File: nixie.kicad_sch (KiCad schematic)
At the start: 51 parts, among them J1 Barrel_Jack, Q1 2N3906, Q2 IRF644, U1 4504, U2 MC34063AP, U3 HV5222PG-G, U4 LM7805_TO220, U5 HV5222PG-G

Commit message: pcb layout update
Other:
- moved on the sheet: N10, N7, N8, N9

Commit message: pcb layout update
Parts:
- added J2: Conn_01x02_Pin, Connector_PinHeader_2.54mm:PinHeader_1x02_P2.54mm_Vertical, symbol Connector:Conn_01x02_Pin
- J1: footprint Connector_PinHeader_2.54mm:PinHeader_1x02_P2.54mm_Vertical -> TerminalBlock_Phoenix:TerminalBlock_Phoenix_MKDS-1,5-2-5.08_1x02_P5.08mm_Horizontal
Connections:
- net GND: now also J2.1 (Pin_1)
- net Vin: now also J2.2 (Pin_2)
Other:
- moved on the sheet: J1
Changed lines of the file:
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@@
 	)
 	(junction
-		(at 29.21 31.75)
+		(at 29.21 29.21)
 		(diameter 0)
 		(color 0 0 0 0)
@@
 	)
 	(junction
-		(at 29.21 26.67)
+		(at 29.21 24.13)
 		(diameter 0)
 		(color 0 0 0 0)
@@
 	(wire
 		(pts
-			(xy 27.94 26.67) (xy 29.21 26.67)
+			(xy 27.94 24.13) (xy 29.21 24.13)
 		)
 		(stroke
@@
 	(polyline
 		(pts
-			(xy 134.62 16.51) (xy 134.62 95.25)
+			(xy 134.62 14.478) (xy 134.62 95.25)
 		)
 		(stroke
@@
 	(wire
 		(pts
-			(xy 29.21 31.75) (xy 27.94 31.75)
+			(xy 29.21 29.21) (xy 27.94 29.21)
 		)
 		(stroke
@@
 	(wire
 		(pts
-			(xy 29.21 26.67) (xy 30.48 26.67)
+			(xy 29.21 24.13) (xy 30.48 24.13)
 		)
 		(stroke
@@
 	(polyline
 		(pts
-			(xy 283.21 16.51) (xy 134.62 16.51)
+			(xy 283.21 14.478) (xy 134.62 14.478)
 		)
 		(stroke
@@
 	(wire
 		(pts
-			(xy 29.21 25.4) (xy 29.21 26.67)
+			(xy 29.21 22.86) (xy 29.21 24.13)
 		)
 		(stroke
@@
 	(wire
 		(pts
-			(xy 29.21 33.02) (xy 29.21 31.75)
+			(xy 29.21 30.48) (xy 29.21 29.21)
 		)
 		(stroke
@@
 	(polyline
 		(pts
-			(xy 283.21 165.1) (xy 283.21 16.51)
+			(xy 283.21 165.1) (xy 283.21 14.478)
 		)
 		(stroke
@@
 	)
 	(rectangle
-		(start 12.7 16.51)
-		(end 132.08 92.71)
+		(start 12.7 14.478)
+		(end 132.08 90.678)
 		(stroke
 			(width 0.2)
@@
 		)
 	)
+	(global_label "Vin"
+		(shape output)
+		(at 35.56 36.83 0)
+		(fields_autoplaced yes)
+		(effects
+			(font
+				(size 1.27 1.27)
+			)
+			(justify left)
+		)
+		(property "Intersheetrefs" "${INTERSHEET_REFS}"
+			(at 41.3876 36.83 0)
+			(effects
+				(font
+					(size 1.27 1.27)
+				)
+				(justify left)
+				(hide yes)
+			)
+		)
+	)
 	(global_label "5V"
 		(shape output)
@@
 	(global_label "Vin"
 		(shape output)
-		(at 30.48 26.67 0)
+		(at 30.48 24.13 0)
 		(fields_autoplaced yes)
 		(effects
@@
 		)
 		(property "Intersheetrefs" "${INTERSHEET_REFS}"
-			(at 36.3076 26.67 0)
+			(at 36.3076 24.13 0)
 			(effects
 				(font
@@
 	(symbol
 		(lib_id "Connector:Barrel_Jack")
-		(at 20.32 29.21 0)
+		(at 20.32 26.67 0)
 		(unit 1)
 		(exclude_from_sim no)
@@
 		(fields_autoplaced yes)
 		(property "Reference" "J1"
-			(at 20.32 20.32 0)
+			(at 20.32 17.78 0)
 			(effects
 				(font
@@
 		)
 		(property "Value" "Barrel_Jack"
-			(at 20.32 22.86 0)
+			(at 20.32 20.32 0)
 			(effects
 				(font
@@
 			)
 		)
-		(property "Footprint" "Connector_PinHeader_2.54mm:PinHeader_1x02_P2.54mm_Vertical"
-			(at 21.59 30.226 0)
+		(property "Footprint" "TerminalBlock_Phoenix:TerminalBlock_Phoenix_MKDS-1,5-2-5.08_1x02_P5.08mm_Horizontal"
+			(at 21.59 27.686 0)
 			(effects
 				(font
@@
 		)
 		(property "Datasheet" "~"
-			(at 21.59 30.226 0)
+			(at 21.59 27.686 0)
 			(effects
 				(font
@@
 		)
 		(property "Description" "DC Barrel Jack"
-			(at 20.32 29.21 0)
+			(at 20.32 26.67 0)
 			(effects
 				(font
@@
 	(symbol
 		(lib_id "power:PWR_FLAG")
-		(at 29.21 25.4 0)
+		(at 29.21 22.86 0)
 		(unit 1)
 		(exclude_from_sim no)
@@
 		(fields_autoplaced yes)
 		(property "Reference" "#FLG01"
-			(at 29.21 23.495 0)
+			(at 29.21 20.955 0)
 			(effects
 				(font
@@
 		)
 		(property "Value" "PWR_FLAG"
-			(at 29.21 20.32 0)
+			(at 29.21 17.78 0)
 			(effects
 				(font
@@
 		)
 		(property "Footprint" ""
-			(at 29.21 25.4 0)
+			(at 29.21 22.86 0)
 			(effects
 				(font
@@
 		)
 		(property "Datasheet" "~"
-			(at 29.21 25.4 0)
+			(at 29.21 22.86 0)
 			(effects
 				(font
@@
 		)
 		(property "Description" "Special symbol for telling ERC where power comes from"
-			(at 29.21 25.4 0)
+			(at 29.21 22.86 0)
 			(effects
 				(font
@@
 	)
 	(symbol
+		(lib_id "Connector:Conn_01x02_Pin")
+		(at 30.48 39.37 0)
+		(mirror x)
+		(unit 1)
+		(exclude_from_sim no)
+		(in_bom yes)
+		(on_board yes)
+		(dnp no)
+		(fields_autoplaced yes)
+		(property "Reference" "J2"
+			(at 29.21 36.8299 0)
+			(effects
+				(font
+					(size 1.27 1.27)
+				)
+				(justify right)
+			)
+		)
+		(property "Value" "Conn_01x02_Pin"
+			(at 29.21 39.3699 0)
+			(effects
+				(font
+					(size 1.27 1.27)
+				)
+				(justify right)
+			)
+		)
+		(property "Footprint" "Connector_PinHeader_2.54mm:PinHeader_1x02_P2.54mm_Vertical"
+			(at 30.48 39.37 0)
+			(effects
+				(font
+					(size 1.27 1.27)
+				)
+				(hide yes)
+			)
+		)
+		(property "Datasheet" "~"
+			(at 30.48 39.37 0)
+			(effects
+				(font
+					(size 1.27 1.27)
+				)
+				(hide yes)
+			)
+		)
+		(property "Description" "Generic connector, single row, 01x02, script generated"
+			(at 30.48 39.37 0)
+			(effects
+				(font
+					(size 1.27 1.27)
+				)
+				(hide yes)
+			)
+		)
+		(pin "1"
+		)
+		(pin "2"
+		)
+		(instances
+			(project ""
+				(path "/4d215aa3-d175-40c4-bbb4-87e7c6a030b1"
+					(reference "J2")
+					(unit 1)
+				)
+			)
+		)
+	)
+	(symbol
 		(lib_id "power:GND")
-		(at 29.21 33.02 0)
+		(at 29.21 30.48 0)
 		(unit 1)
 		(exclude_from_sim no)
@@
 		(dnp no)
 		(property "Reference" "#PWR03"
-			(at 29.21 39.37 0)
+			(at 29.21 36.83 0)
 			(effects
 				(font
@@
 		)
 		(property "Value" "GND"
-			(at 29.21 37.084 0)
+			(at 29.21 34.544 0)
 			(effects
 				(font
@@
 		)
 		(property "Footprint" ""
-			(at 29.21 33.02 0)
+			(at 29.21 30.48 0)
 			(effects
 				(font
@@
 		)
 		(property "Datasheet" ""
-			(at 29.21 33.02 0)
+			(at 29.21 30.48 0)
 			(effects
 				(font
@@
 		)
 		(property "Description" "Power symbol creates a global label with name \"GND\" , ground"
-			(at 29.21 33.02 0)
+			(at 29.21 30.48 0)
 			(effects
 				(font
@@
 	(symbol
 		(lib_id "power:PWR_FLAG")
-		(at 29.21 31.75 270)
+		(at 29.21 29.21 270)
 		(unit 1)
 		(exclude_from_sim no)
@@
 		(fields_autoplaced yes)
 		(property "Reference" "#FLG02"
-			(at 31.115 31.75 0)
+			(at 31.115 29.21 0)
 			(effects
 				(font
@@
 		)
 		(property "Value" "PWR_FLAG"
-			(at 33.02 31.7499 90)
+			(at 33.02 29.2099 90)
 			(effects
 				(font
@@
 		)
 		(property "Footprint" ""
-			(at 29.21 31.75 0)
+			(at 29.21 29.21 0)
 			(effects
 				(font
@@
 		)
 		(property "Datasheet" "~"
-			(at 29.21 31.75 0)
+			(at 29.21 29.21 0)
 			(effects
 				(font
@@
 		)
 		(property "Description" "Special symbol for telling ERC where power comes from"
-			(at 29.21 31.75 0)
+			(at 29.21 29.21 0)
 			(effects
 				(font
@@
 					(unit 1)
 				)
+			)
+		)
+	)
+	(symbol
+		(lib_id "power:GND")
+		(at 35.56 39.37 0)
+		(unit 1)
+		(exclude_from_sim no)
+		(in_bom yes)
+		(on_board yes)
+		(dnp no)
+		(property "Reference" "#PWR032"
+			(at 35.56 45.72 0)
+			(effects
+				(font
+					(size 1.27 1.27)
+				)
+				(hide yes)
+			)
+		)
+		(property "Value" "GND"
+			(at 35.56 43.434 0)
+			(effects
+				(font
+					(size 1.27 1.27)
+				)
+			)
+		)
+		(property "Footprint" ""
+			(at 35.56 39.37 0)
+			(effects
+				(font
+					(size 1.27 1.27)
+				)
+				(hide yes)
+			)
+		)
+		(property "Datasheet" ""
+			(at 35.56 39.37 0)
+			(effects
+				(font
+					(size 1.27 1.27)
+				)
+				(hide yes)
+			)
+		)
+		(property "Description" "Power symbol creates a global label with name \"GND\" , ground"
+			(at 35.56 39.37 0)
+			(effects
+				(font
+					(size 1.27 1.27)
+				)
+				(hide yes)
+			)
+		)
+		(pin "1"
+		)
+		(instances
+			(project "nixie"
+				(path "/4d215aa3-d175-40c4-bbb4-87e7c6a030b1"
+					(reference "#PWR032")
+					(unit 1)
+				)

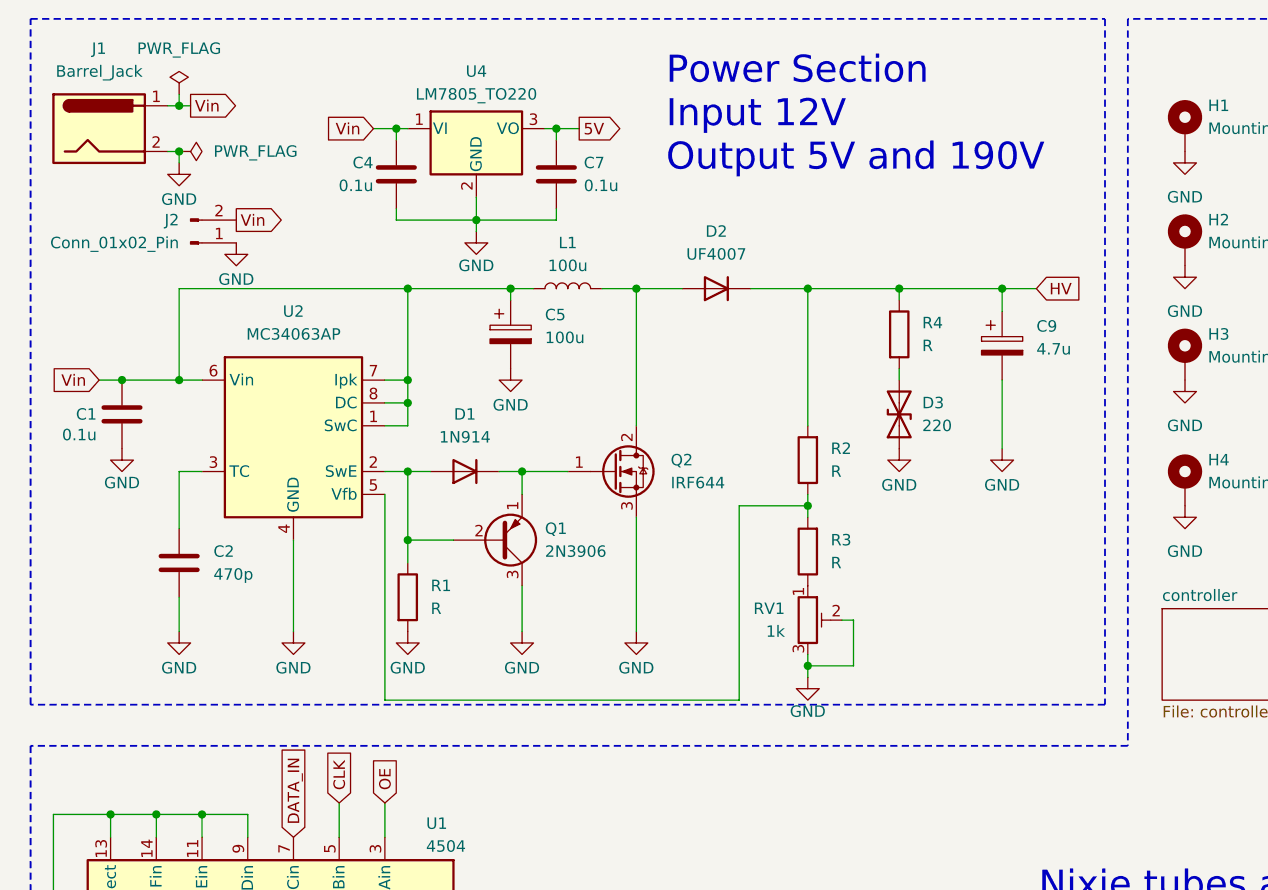
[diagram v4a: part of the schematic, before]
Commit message: added 3D model, added missing component values, improved interactive bom
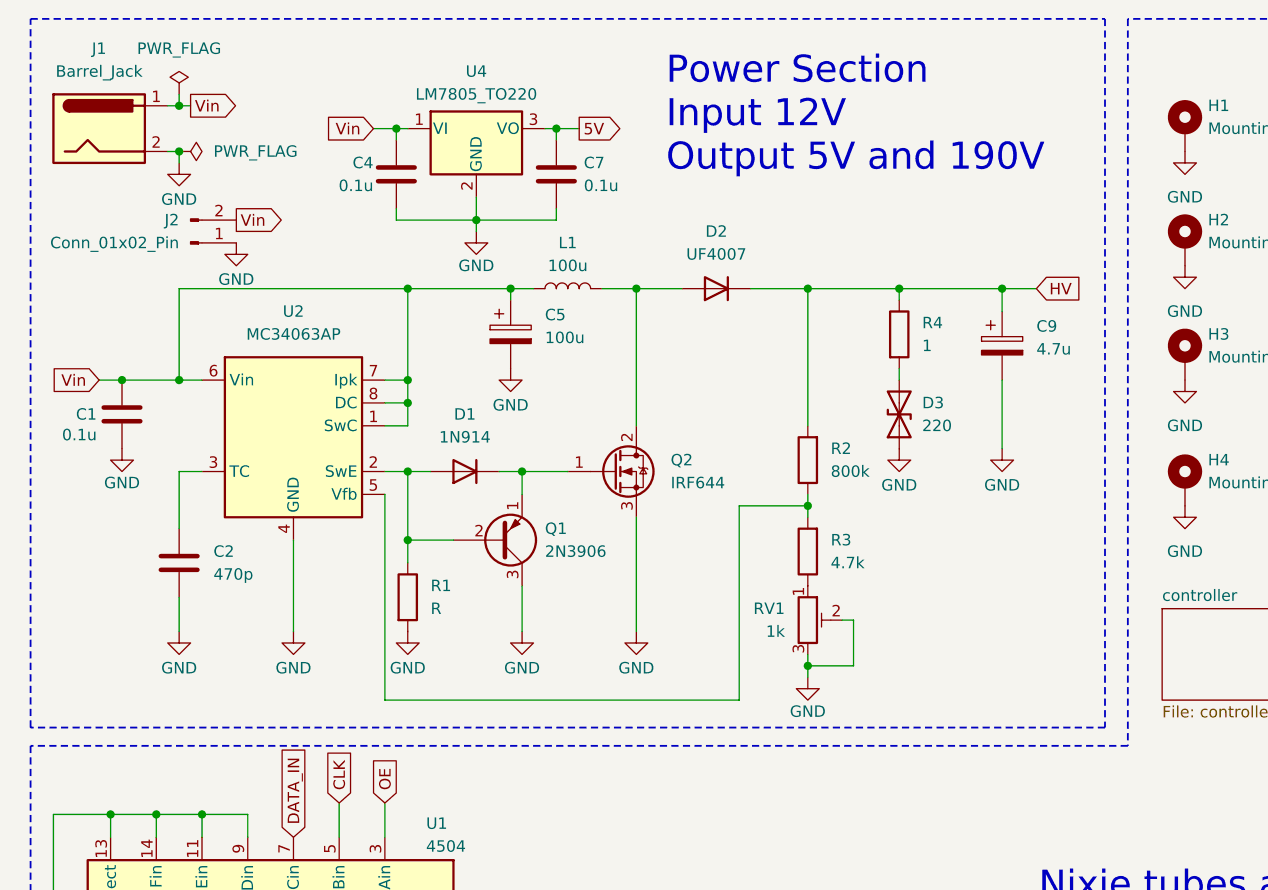
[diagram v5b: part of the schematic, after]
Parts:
- R2: value R -> 800k
- R3: value R -> 4.7k
- R4: value R -> 1
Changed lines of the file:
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@@
 	(rectangle
 		(start 12.7 14.478)
-		(end 132.08 90.678)
+		(end 132.08 93.218)
 		(stroke
 			(width 0.2)
@@
 			)
 		)
-		(property "Value" "R"
+		(property "Value" "4.7k"
 			(at 101.6 74.9299 0)
 			(effects
@@
 			)
 		)
-		(property "Value" "R"
+		(property "Value" "800k"
 			(at 101.6 64.7699 0)
 			(effects
@@
 			)
 		)
-		(property "Value" "R"
+		(property "Value" "1"
 			(at 111.76 50.7999 0)
 			(effects

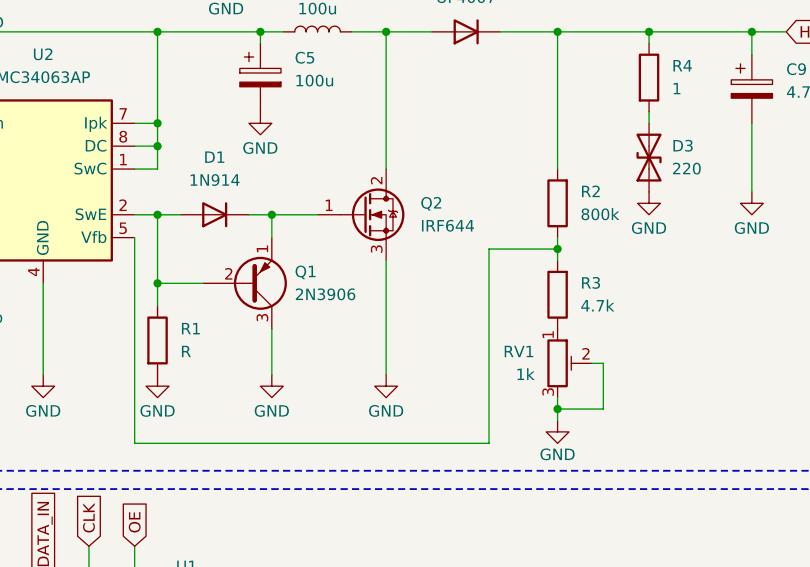
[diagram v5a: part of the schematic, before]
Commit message: updated component values
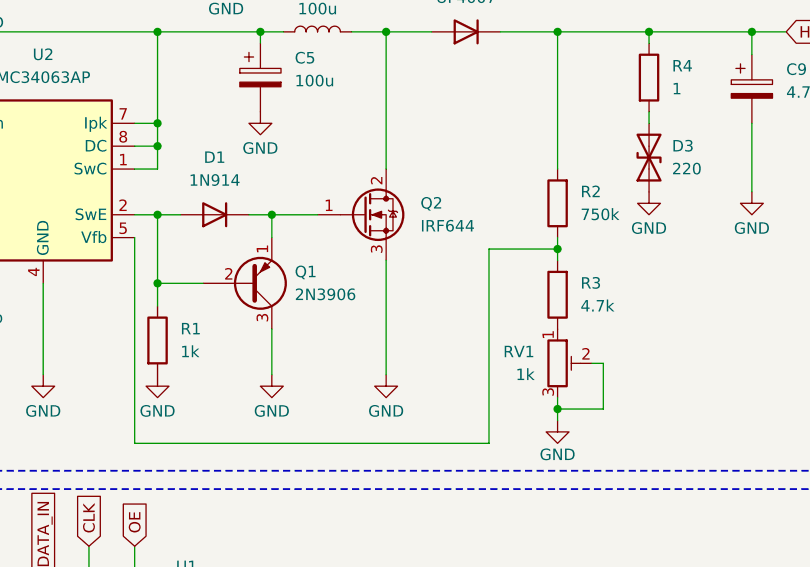
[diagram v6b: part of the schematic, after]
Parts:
- R1: value R -> 1k
- R2: value 800k -> 750k
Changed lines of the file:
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@@
 			)
 		)
-		(property "Value" "R"
+		(property "Value" "1k"
 			(at 57.15 80.0099 0)
 			(effects
@@
 			)
 		)
-		(property "Value" "800k"
+		(property "Value" "750k"
 			(at 101.6 64.7699 0)
 			(effects
